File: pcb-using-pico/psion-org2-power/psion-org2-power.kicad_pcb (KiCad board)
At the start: 2 copper layers, 71.8 x 103.1 mm, 14 parts, among them J1 Conn_02x08_Odd_Even, J2 Conn_02x08_Odd_Even, J3 Conn_01x27_Female, J4 Conn_02x08_Odd_Even, U6 74LS245, U7 74LS245

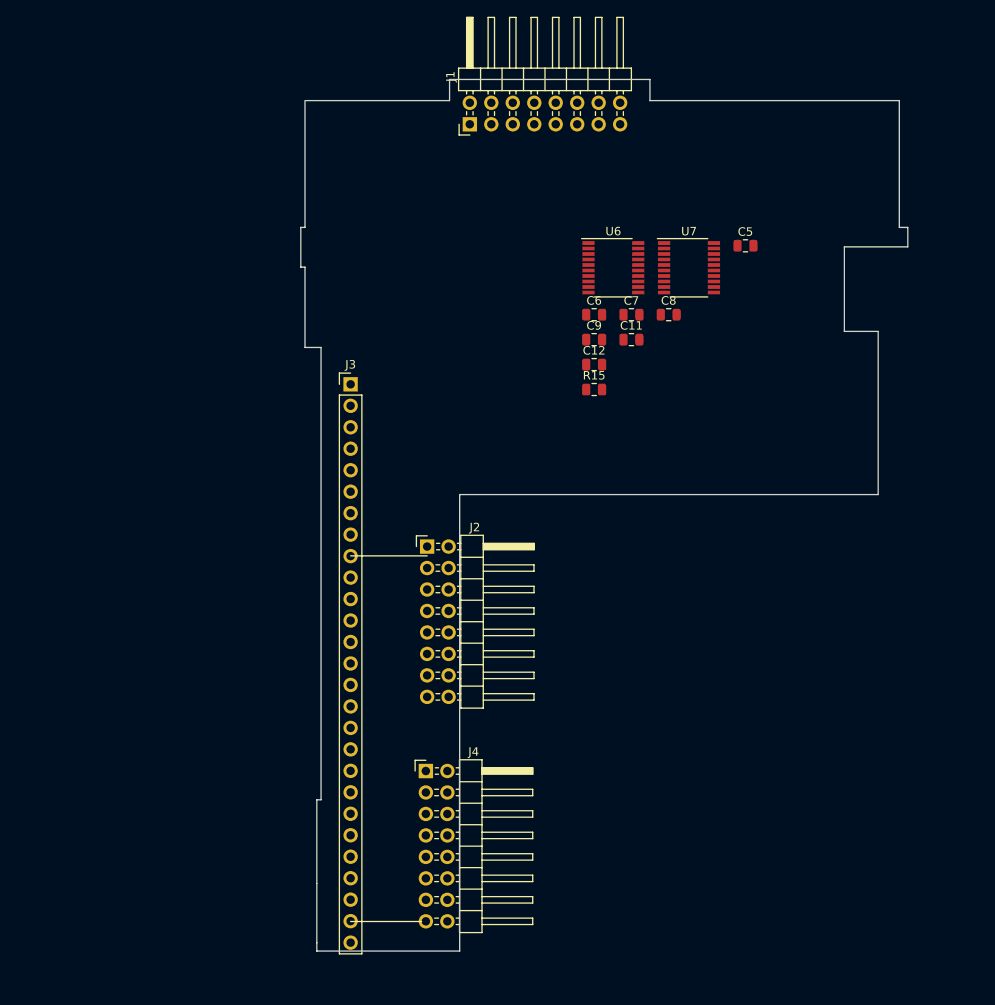
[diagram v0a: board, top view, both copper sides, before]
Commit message: Added second connector, eeprom on power pcb
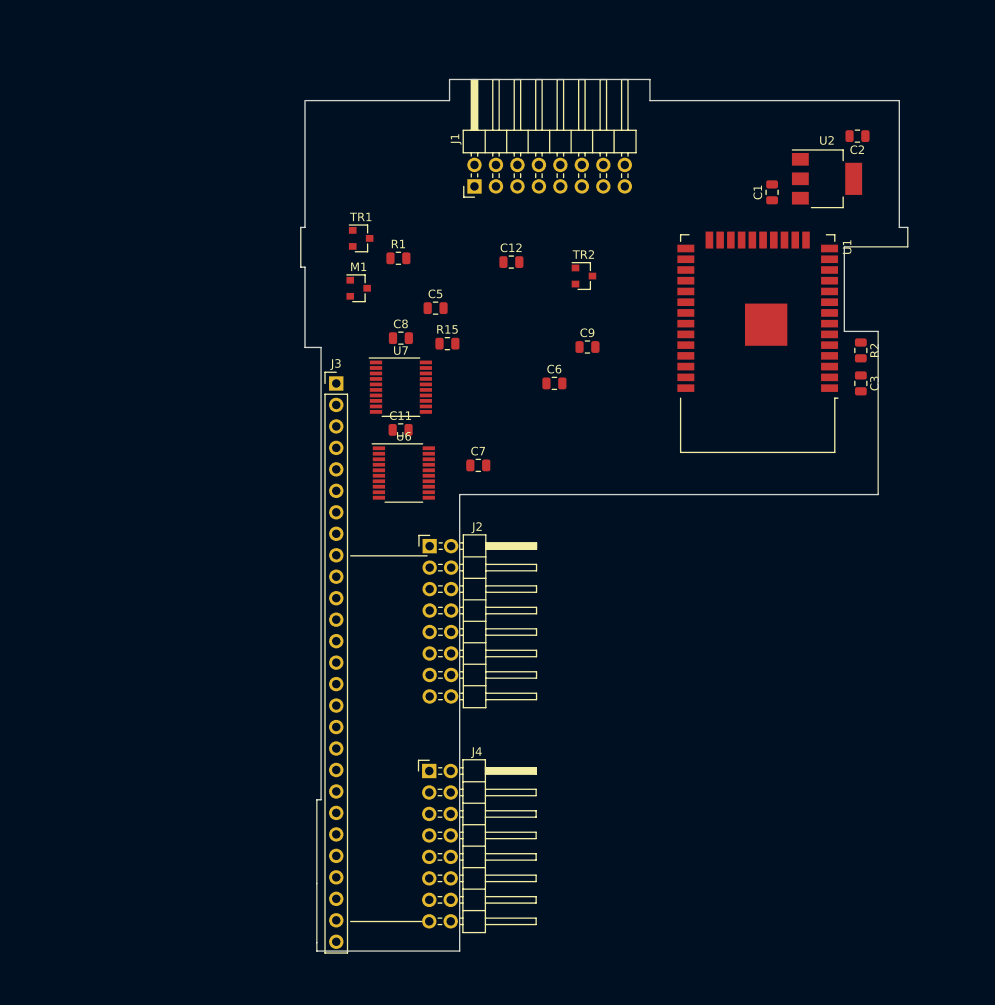
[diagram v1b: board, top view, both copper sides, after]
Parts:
- added C1: C_Small, Capacitor_SMD:C_0805_2012Metric, F.Cu at (134.2, 40.2)
- added C2: C_Small, Capacitor_SMD:C_0805_2012Metric, F.Cu at (144.2, 33.6)
- added C3: C_Small, Capacitor_SMD:C_0805_2012Metric, F.Cu at (144.7, 62.9)
- added M1: P-CHANNEL-MOSFET, Package_TO_SOT_SMD:SOT-23, F.Cu at (85.2, 51.6)
- added R1: 100k, Resistor_SMD:R_0805_2012Metric, F.Cu at (90.0, 48.0)
- added R2: R_Small, Resistor_SMD:R_0805_2012Metric, F.Cu at (144.7, 59.0)
- added TR1: Si2302CDS-n-channel, Package_TO_SOT_SMD:SOT-23, F.Cu at (85.5, 45.7)
- added TR2: Si2302CDS-n-channel, Package_TO_SOT_SMD:SOT-23, F.Cu at (111.9, 50.1)
- added U1: ESP32-WROOM-32, RF_Module:ESP32-WROOM-32, F.Cu at (132.4, 55.1)
- added U2: AMS1117-3.3, Package_TO_SOT_SMD:SOT-223-3_TabPin2, F.Cu at (140.7, 38.6)
- moved C5 37.4 mm to (94.3, 54.0)
- moved U7 36.9 mm to (90.2, 63.3)
- moved U6 34.7 mm to (90.6, 73.5)
- moved C8 31.8 mm to (90.2, 57.5)
- moved C11 29.3 mm to (90.2, 68.3)
- moved C7 25.4 mm to (99.4, 72.5)
- moved R15 18.2 mm to (95.8, 58.1)
- moved C12 15.6 mm to (103.3, 48.5)
- moved C6 9.39 mm to (108.4, 62.9)
- moved J1 7.37 mm to (99.0, 39.5)
- moved J3 1.70 mm to (82.6, 62.9)
- moved C9 1.18 mm to (112.3, 58.5)
- moved J4 0.40 mm to (93.6, 108.7)
- moved J2 0.30 mm to (93.7, 82.1)
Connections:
- J2 pad 15: (no net) -> VCC_SLOT
- J3 pad 17: (no net) -> LS_DIR
- J3 pad 19: (no net) -> ESP_ON
- J3 pad 24: (no net) -> 5V_ON
- J3 pad 25: (no net) -> 5V
- J3 pad 26: (no net) -> VBAT
- J4 pad 15: (no net) -> VCC_SLOT

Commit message: Start of PCB layout
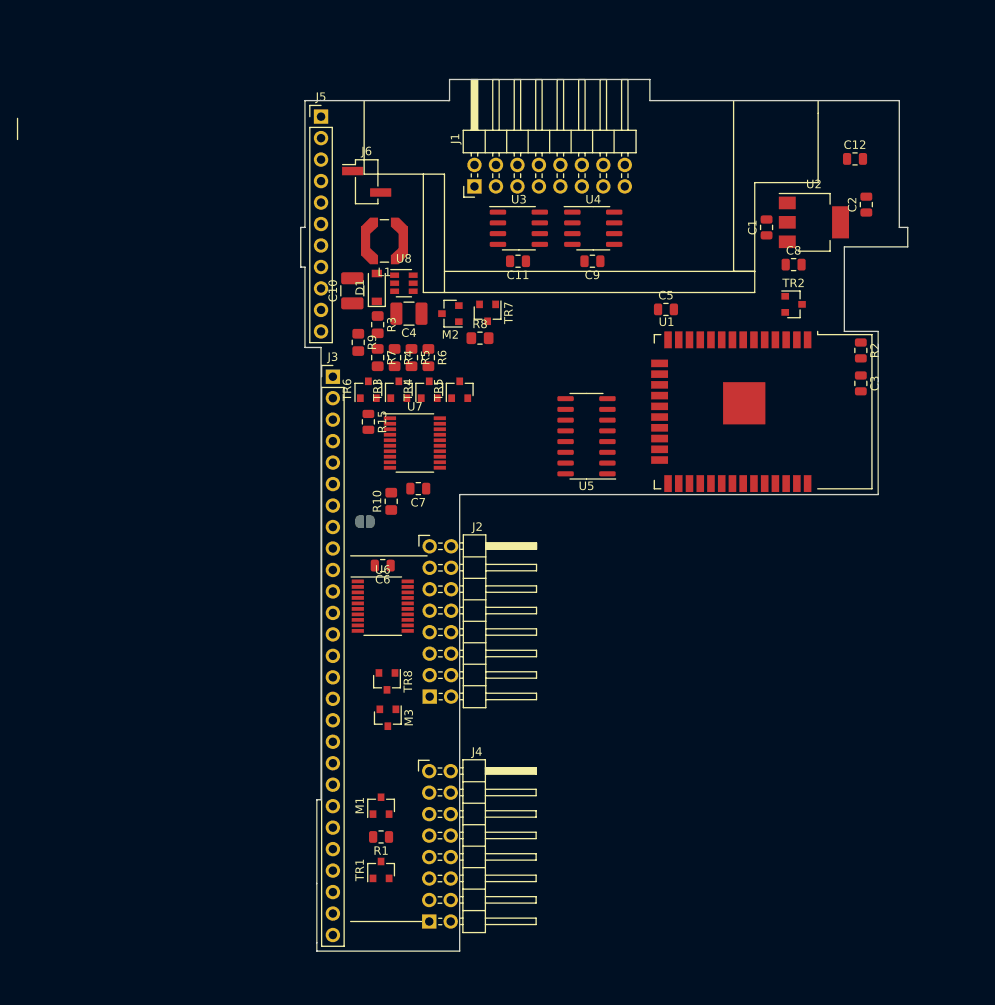
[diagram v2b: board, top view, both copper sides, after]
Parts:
- added C10: 22uF, Capacitor_SMD:C_1210_3225Metric_Pad1.42x2.65mm_HandSolder, F.Cu at (84.5, 51.9)
- added C4: 22uF, Capacitor_SMD:C_1210_3225Metric_Pad1.42x2.65mm_HandSolder, F.Cu at (91.2, 54.6)
- added D1: D, Diode_SMD:D_SOD-123, F.Cu at (87.4, 51.5)
- added J5: Conn_01x11_Female, Connector_PinHeader_2.54mm:PinHeader_1x11_P2.54mm_Vertical, F.Cu at (80.8, 31.3)
- added J6: Conn_01x02_Female, Connector_PinHeader_2.54mm:PinHeader_1x02_P2.54mm_Vertical_SMD_Pin1Left, F.Cu at (86.2, 39.0)
- added JP1: SolderJumper_2_Open, Jumper:SolderJumper-2_P1.3mm_Open_RoundedPad1.0x1.5mm, B.Cu at (86.0, 79.2)
- added L1: 22uH, Inductor_SMD:L_Coilcraft_LPS5030, F.Cu at (88.3, 46.0)
- added M2: P-CHANNEL-MOSFET, Package_TO_SOT_SMD:SOT-23, F.Cu at (96.1, 54.6)
- added M3: AO3401, Package_TO_SOT_SMD:SOT-23, F.Cu at (88.7, 102.4)
- added R10: R_Small, Resistor_SMD:R_0805_2012Metric_Pad1.15x1.40mm_HandSolder, F.Cu at (89.1, 76.8)
- added R3: 120k, Resistor_SMD:R_0805_2012Metric_Pad1.15x1.40mm_HandSolder, F.Cu at (87.5, 55.9)
- added R4: 18k, Resistor_SMD:R_0805_2012Metric_Pad1.15x1.40mm_HandSolder, F.Cu at (89.5, 59.8)
- added R5: 18k, Resistor_SMD:R_0805_2012Metric_Pad1.15x1.40mm_HandSolder, F.Cu at (91.5, 59.8)
- added R6: 18k, Resistor_SMD:R_0805_2012Metric_Pad1.15x1.40mm_HandSolder, F.Cu at (93.5, 59.8)
- added R7: 18k, Resistor_SMD:R_0805_2012Metric_Pad1.15x1.40mm_HandSolder, F.Cu at (87.5, 59.8)
- added R8: 100k, Resistor_SMD:R_0805_2012Metric_Pad1.15x1.40mm_HandSolder, F.Cu at (99.6, 57.5)
- added R9: 100k, Resistor_SMD:R_0805_2012Metric_Pad1.15x1.40mm_HandSolder, F.Cu at (85.2, 58.0)
- added TR3: AO3400, Package_TO_SOT_SMD:SOT-23, F.Cu at (90.0, 63.6)
- added TR4: AO3400, Package_TO_SOT_SMD:SOT-23, F.Cu at (93.6, 63.6)
- added TR5: AO3400, Package_TO_SOT_SMD:SOT-23, F.Cu at (97.2, 63.6)
- added TR6: AO3400, Package_TO_SOT_SMD:SOT-23, F.Cu at (86.4, 63.6)
- added TR7: AO3400, Package_TO_SOT_SMD:SOT-23, F.Cu at (100.5, 54.5)
- added TR8: AO3400, Package_TO_SOT_SMD:SOT-23, F.Cu at (88.6, 98.1)
- added U3: CAT24C256, Package_SO:SOIC-8_3.9x4.9mm_P1.27mm, F.Cu at (104.2, 44.5)
- added U4: CAT24C256, Package_SO:SOIC-8_3.9x4.9mm_P1.27mm, F.Cu at (113.0, 44.5)
- added U5: 74HC595, Package_SO:SOIC-16_3.9x9.9mm_P1.27mm, F.Cu at (112.2, 69.1)
- added U8: Regulator_Switching_MT3608, Package_TO_SOT_SMD:SOT-23-6, F.Cu at (90.6, 51.0)
- J2, J4: footprint Connector_PinHeader_2.54mm:PinHeader_2x08_P2.54mm_Horizontal -> ajm_kicad:PinHeader_2x08_P2.54mm_Horizontal_psionSide
- moved TR1 74.7 mm to (87.9, 120.4), turned to 90 degrees
- moved R1 68.5 mm to (87.9, 116.5), turned to 180 degrees
- moved M1 61.3 mm to (87.9, 112.8), turned to 90 degrees
- moved C8 47.3 mm to (136.7, 48.8)
- moved C12 42.4 mm to (144.0, 36.3)
- moved C6 29.6 mm to (88.1, 84.4), turned to 180 degrees
- moved C5 27.3 mm to (121.6, 54.1)
- moved TR2 25.0 mm to (136.7, 53.5)
- moved C11 24.3 mm to (104.1, 48.4), turned to 180 degrees
- moved U6 15.9 mm to (88.1, 89.2)
- moved R15 13.2 mm to (86.4, 67.4), turned to 270 degrees
- moved U1 11.3 mm to (130.1, 66.2), turned to 270 degrees
- moved C9 10.2 mm to (112.9, 48.4), turned to 180 degrees
- moved C2 8.17 mm to (145.3, 41.7), turned to 90 degrees
- moved C7 7.61 mm to (92.3, 75.3), turned to 180 degrees
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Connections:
- C1 pad 1: VBAT -> VBAT_SWITCHED2
- J1 pad 1: (no net) -> P_SD7
- J1 pad 10: (no net) -> P_SCLK
- J1 pad 11: (no net) -> EXT_PWR_IN
- J1 pad 12: (no net) -> P_SS3
- J1 pad 13: (no net) -> VCC_SLOT
- J1 pad 14: (no net) -> EX_ON
- J1 pad 15: (no net) -> P_SOE
- J1 pad 16: (no net) -> P_SMR
- J1 pad 2: (no net) -> P_SD0
- J1 pad 3: (no net) -> P_SD6
- J1 pad 4: (no net) -> P_SD1
- J1 pad 5: (no net) -> P_SD5
- J1 pad 6: (no net) -> P_SD2
- J1 pad 7: (no net) -> P_SD4
- J1 pad 8: (no net) -> P_SD3
- J1 pad 9: (no net) -> GND
- J2 pad 16: (no net) -> VPP
- J3 pad 18: (no net) -> SD_OE
- J3 pad 19: ESP_ON -> SC_OE
- J3 pad 20: (no net) -> EXT_PWR_IN
- J3 pad 21: (no net) -> ESP_ON
- J3 pad 22: (no net) -> EX_ON
- J3 pad 23: (no net) -> VBAT_SWITCHED2
- J4 pad 16: (no net) -> VPP
- U1 pad 27: (no net) -> PICO_TX
- U1 pad 28: (no net) -> PICO_RX
- U2 pad 3: VBAT -> VBAT_SWITCHED2
- U6 pad 12: (no net) -> P_SS3
- U6 pad 19: GND -> SD_OE
- U7 pad 19: GND -> SC_OE
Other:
- outline, holes or cut-outs redrawn

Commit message: First main PCB layout
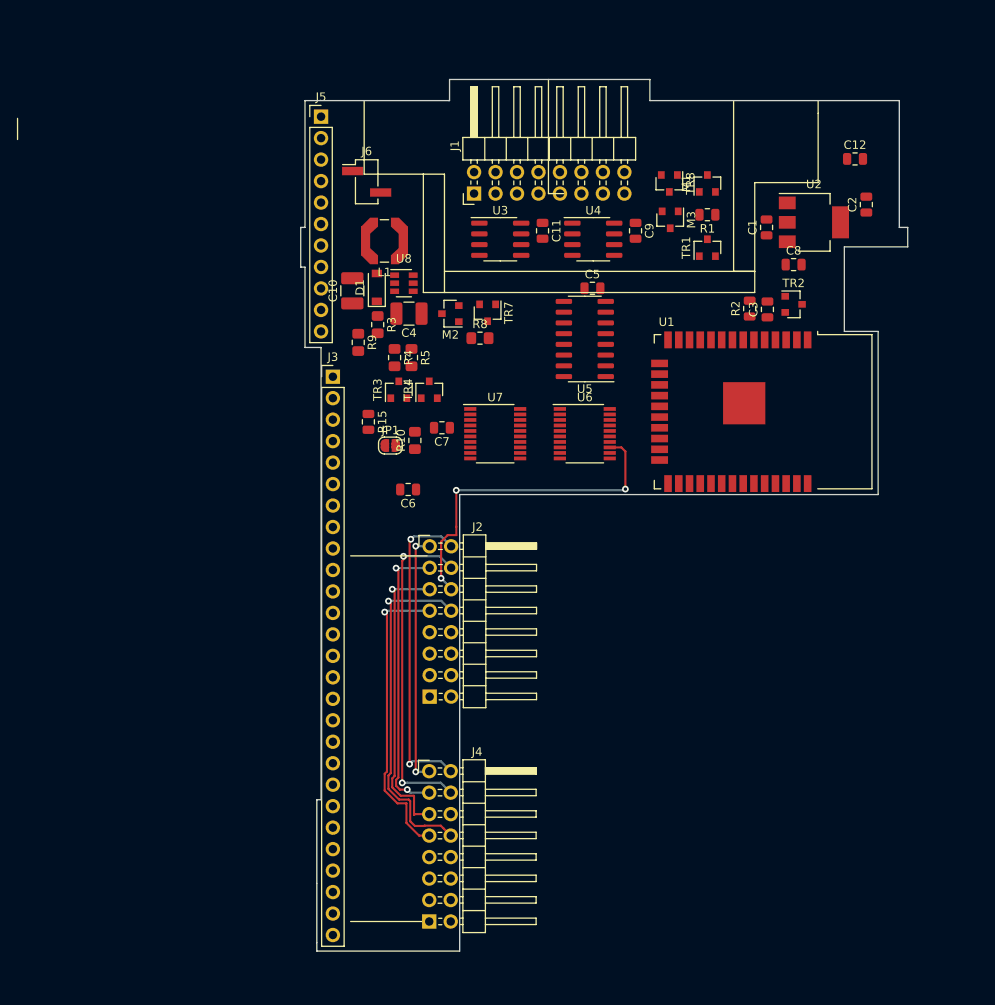
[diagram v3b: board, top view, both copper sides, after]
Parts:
- removed R6, R7: 18k, Resistor_SMD:R_0805_2012Metric_Pad1.15x1.40mm_HandSolder
- removed TR5, TR6: AO3400, Package_TO_SOT_SMD:SOT-23
- JP1: moved to F.Cu
- moved TR1 83.1 mm to (126.5, 46.8)
- moved M1 83.1 mm to (126.5, 39.2)
- moved R1 83.1 mm to (126.5, 42.9)
- moved M3 67.7 mm to (122.1, 43.5)
- moved TR8 67.7 mm to (122.0, 39.2)
- moved U6 31.4 mm to (112.0, 68.8)
- moved C3 14.1 mm to (133.6, 54.1), turned to 90 degrees
- moved R2 14.1 mm to (131.5, 54.0), turned to 90 degrees
- moved U5 11.5 mm to (112.0, 57.6)
- moved U7 9.56 mm to (101.4, 68.8)
- moved C6 9.49 mm to (91.1, 75.4)
- moved JP1 9.49 mm to (89.0, 70.2)
- moved C5 9.05 mm to (112.9, 51.6)
- moved R10 7.73 mm to (91.9, 69.6)
- moved C7 7.73 mm to (95.1, 68.1)
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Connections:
- J3 pad 10: SPGM -> (no net)
- J3 pad 14: SS1 -> (no net)
- J3 pad 15: SS2 -> (no net)
- J3 pad 16: SS3 -> (no net)
- U5 pad 2: (no net) -> SPGM
- U5 pad 3: (no net) -> SS1
- U5 pad 4: (no net) -> SS2
- U5 pad 5: (no net) -> SS3
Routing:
- net P_SCLK: track 0.00 -> 41.5 mm, vias 0 -> 1
- net P_SS2: track 0.00 -> 40.1 mm, vias 0 -> 3
- net P_SPGM: track 0.00 -> 39.6 mm, vias 0 -> 2
- net VPP: track 0.00 -> 37.5 mm, vias 0 -> 2
- net P_SMR: track 0.00 -> 35.6 mm, vias 0 -> 1
- net P_SOE: track 0.00 -> 35.3 mm, vias 0 -> 1
- net GND: track 0.00 -> 34.2 mm, vias 0 -> 2
- net VCC_SLOT: track 0.00 -> 30.0 mm, vias 0 -> 2

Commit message: First layouts for fabrication
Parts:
- removed C10, C4: 22uF, Capacitor_SMD:C_1210_3225Metric_Pad1.42x2.65mm_HandSolder
- removed C11, C12, C9: 100n, Capacitor_SMD:C_0805_2012Metric
- removed C5: 1u, Capacitor_SMD:C_0805_2012Metric
- removed D1: D, Diode_SMD:D_SOD-123
- removed JP1: SolderJumper_2_Open, Jumper:SolderJumper-2_P1.3mm_Open_RoundedPad1.0x1.5mm
- removed L1: 22uH, Inductor_SMD:L_Coilcraft_LPS5030
- removed M2: P-CHANNEL-MOSFET, Package_TO_SOT_SMD:SOT-23
- removed M3: AO3401, Package_TO_SOT_SMD:SOT-23
- removed R10: R_Small, Resistor_SMD:R_0805_2012Metric_Pad1.15x1.40mm_HandSolder
- removed R3: 120k, Resistor_SMD:R_0805_2012Metric_Pad1.15x1.40mm_HandSolder
- removed R4, R5: 18k, Resistor_SMD:R_0805_2012Metric_Pad1.15x1.40mm_HandSolder
- removed R8, R9: 100k, Resistor_SMD:R_0805_2012Metric_Pad1.15x1.40mm_HandSolder
- removed TR3, TR4, TR7, TR8: AO3400, Package_TO_SOT_SMD:SOT-23
- removed U8: Regulator_Switching_MT3608, Package_TO_SOT_SMD:SOT-23-6
- moved C8 29.0 mm to (113.7, 66.5), turned to 90 degrees
- moved C7 27.7 mm to (107.5, 43.3), turned to 0 degrees
- moved C6 14.7 mm to (98.5, 62.7), turned to 270 degrees
- moved U7 10.3 mm to (92.9, 63.0), turned to 90 degrees
- moved U5 5.07 mm to (107.1, 56.3), turned to 270 degrees
- moved U6 4.08 mm to (108.5, 66.7), turned to 270 degrees
- moved R2 2.22 mm to (133.7, 54.3)
- moved C3 2.01 mm to (131.6, 54.3)
- moved R15 1.84 mm to (87.6, 66.0), turned to 0 degrees
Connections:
- J2 pad 14: P_SPGM -> (no net)
- J2 pad 16: VPP -> (no net)
- J4 pad 14: P_SPGM -> (no net)
- J4 pad 16: VPP -> (no net)
- U5 pad 1: VPP_X2 -> (no net)
- U5 pad 15: VPP_X1 -> (no net)
- U5 pad 2: SPGM -> (no net)
- U5 pad 6: VPP_SLOT_ON -> (no net)
- U5 pad 7: VPP_ON -> (no net)
- U6 pad 18: P_SPGM -> (no net)
- U6 pad 2: SPGM -> (no net)
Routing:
- net GND: track 34.2 -> 277.0 mm, vias 2 -> 23
- net +3V3: track 0.00 -> 199.6 mm, vias 0 -> 15
- net EX_ON: track 0.00 -> 170.2 mm, vias 0 -> 2
- net VCC_SLOT: track 30.0 -> 172.5 mm, vias 2 -> 6
- net 5V: track 0.00 -> 135.4 mm, vias 0 -> 2
- net VBAT: track 0.00 -> 128.7 mm, vias 0 -> 4
- net P_SD2: track 0.00 -> 122.3 mm, vias 0 -> 3
- net VBAT_SWITCHED2: track 0.00 -> 122.3 mm, vias 0 -> 4
- net ESP_ON: track 0.00 -> 121.7 mm, vias 0 -> 3
- net P_SD3: track 0.00 -> 120.3 mm, vias 0 -> 5
- net P_SD5: track 0.00 -> 116.1 mm, vias 0 -> 7
- net P_SD1: track 0.00 -> 115.5 mm, vias 0 -> 4
- net 5V_ON: track 0.00 -> 114.8 mm, vias 0 -> 4
- net P_SD4: track 0.00 -> 114.2 mm, vias 0 -> 4
- net P_SD0: track 0.00 -> 114.1 mm, vias 0 -> 4
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- added copper zone on F.Cu, net GND
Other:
- board text added: "GND"
- board text added: "VBAT"

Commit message: Small updates and sent to fab
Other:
- board text added: "Psion Organiser 2 Re Creation Power Board Nov 2021 V1.0 menadue@gmail.com"
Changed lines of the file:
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@@
   (general
     (thickness 1.6)
-    (drawings 46)
+    (drawings 47)
     (tracks 2455)
     (zones 0)
@@
     )
   )
+  (gr_text "Psion Organiser 2 Re Creation Power Board\nNov 2021 \nV1.0  \nmenadue@gmail.com\n" (at 87.5 103.4 90) (layer F.SilkS)
+    (effects (font (size 1 1) (thickness 0.15)))
+  )
   (gr_text GND (at 89.3 41.5) (layer F.SilkS)

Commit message: V1.1 started
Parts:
- added C10: 100n, Capacitor_SMD:C_0805_2012Metric, F.Cu at (85.9, 57.4)
- added C11: 100n, Capacitor_SMD:C_0805_2012Metric, F.Cu at (117.9, 45.1)
- added C12: 4u7, Capacitor_SMD:C_0805_2012Metric, F.Cu at (124.9, 54.4)
- added C4: C_Small, Capacitor_SMD:C_0805_2012Metric, F.Cu at (144.0, 38.3)
- added C5: C_Small, Capacitor_SMD:C_0805_2012Metric, F.Cu at (147.7, 39.1)
- added C9: 100n, Capacitor_SMD:C_0805_2012Metric, F.Cu at (113.6, 61.2)
- added D1: 3V0, Diode_SMD:D_SOD-123, F.Cu at (122.3, 40.9)
- added D2: 4V7, Diode_SMD:D_SOD-123, F.Cu at (139.9, 48.8)
- added J7: Conn_01x03_Female, Connector_PinHeader_2.54mm:PinHeader_1x03_P2.54mm_Vertical_SMD_Pin1Left, B.Cu at (133.7, 70.2)
- added JP1: Jumper_NO_Small, Jumper:SolderJumper-2_P1.3mm_Open_RoundedPad1.0x1.5mm, B.Cu at (125.8, 70.8)
- added M2: P-CHANNEL-MOSFET, Package_TO_SOT_SMD:SOT-23, F.Cu at (127.9, 54.2)
- added R10: 100k, Resistor_SMD:R_0805_2012Metric, F.Cu at (90.7, 127.8)
- added R11: 100k, Resistor_SMD:R_0805_2012Metric, F.Cu at (88.8, 127.8)
- added R12: 100k, Resistor_SMD:R_0805_2012Metric, F.Cu at (125.8, 36.1)
- added R13: 100k, Resistor_SMD:R_0805_2012Metric, F.Cu at (122.6, 43.2)
- added R14: 100k, Resistor_SMD:R_0805_2012Metric, F.Cu at (122.8, 47.0)
- added R16: 10k, Resistor_SMD:R_0805_2012Metric, F.Cu at (140.1, 50.9)
- added R17: 10k, Resistor_SMD:R_0805_2012Metric, F.Cu at (118.3, 54.7)
- added R3: R_Small, Resistor_SMD:R_0805_2012Metric, F.Cu at (103.2, 66.1)
- added R4: 100k, Resistor_SMD:R_0805_2012Metric, F.Cu at (98.3, 59.2)
- added R5: 100k, Resistor_SMD:R_0805_2012Metric, F.Cu at (85.3, 120.3)
- added R6: 100k, Resistor_SMD:R_0805_2012Metric, F.Cu at (90.6, 40.2)
- added R7: 100k, Resistor_SMD:R_0805_2012Metric, F.Cu at (90.6, 46.0)
- added R8: 100k, Resistor_SMD:R_0805_2012Metric, F.Cu at (85.0, 127.8)
- added R9: 100k, Resistor_SMD:R_0805_2012Metric, F.Cu at (86.9, 127.8)
- added TR3: Si2302CDS-n-channel, Package_TO_SOT_SMD:SOT-23, F.Cu at (117.4, 58.2)
- added U8: AMS1117-5.0, Package_TO_SOT_SMD:SOT-223-3_TabPin2, F.Cu at (144.6, 33.5)
- C3: value C_Small -> 100nF
- TR2: value Si2302CDS-n-channel -> Si2302CDS-n-ch
- moved TR2 22.3 mm to (122.2, 36.6)
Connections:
- C1 pad 1: VBAT_SWITCHED2 -> ESP_IN_POWER
- C3 pad 2: Net-(C3-Pad2) -> GND
- J2 pad 14: (no net) -> P_SPGM
- J3 pad 10: (no net) -> SPGM
- J3 pad 22: EX_ON -> EX_ON_INV
- J4 pad 14: (no net) -> P_SPGM
- TR2 pad 1: ESP_ON -> EX_ON
- TR2 pad 3: Net-(C3-Pad2) -> EX_ON_INV
- U1 pad 1: Net-(C3-Pad2) -> GND
- U1 pad 15: Net-(C3-Pad2) -> GND
- U1 pad 25: (no net) -> Net-(JP1-Pad1)
- U1 pad 34: (no net) -> Net-(J7-Pad3)
- U1 pad 35: (no net) -> Net-(J7-Pad1)
- U1 pad 38: Net-(C3-Pad2) -> GND
- U1 pad 39: Net-(C3-Pad2) -> GND
- U2 pad 3: VBAT_SWITCHED2 -> ESP_IN_POWER
- U6 pad 18: (no net) -> P_SPGM
- U6 pad 2: (no net) -> SPGM
- U6 pad 9: (no net) -> Net-(R3-Pad1)
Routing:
- net EX_ON_INV: track 0.00 -> 172.1 mm, vias 0 -> 5
- net GND: track 277.0 -> 444.1 mm, vias 23 -> 34
- net EX_ON: track 170.2 -> 17.1 mm, vias 2 -> 0
- net P_SPGM: track 0.00 -> 106.4 mm, vias 0 -> 2
- net SPGM: track 0.00 -> 53.6 mm, vias 0 -> 2
- net Net-(C3-Pad2): track 51.5 -> 0.00 mm
- net VBAT: track 128.7 -> 177.3 mm, vias 4 -> 7
- net Net-(D2-Pad2): track 0.00 -> 32.0 mm, vias 0 -> 4
- net 5V: track 135.4 -> 165.7 mm, vias 2 -> 4
- net VBAT_SWITCHED2: track 122.3 -> 149.5 mm, vias 4 -> 7
- net ESP_IN_POWER: track 0.00 -> 18.4 mm, vias 0 -> 2
- net ESP_ON: track 121.7 -> 108.2 mm, vias 3 -> 5
- net Net-(R3-Pad1): track 0.00 -> 8.02 mm, vias 0 -> 2
- net P_SD3: track 120.3 -> 128.2 mm
- net Net-(C12-Pad1): track 8.93 -> 16.2 mm
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- removed copper zone on F.Cu, net GND
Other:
- board text added: "Psion Organiser 2 Re-Creation Power Board Dec 2021 V1.1 menadue@gmail.com"
- board text removed: "Psion Organiser 2 Re Creation Power Board Nov 2021 V1.0 menadue@gmail.com"
